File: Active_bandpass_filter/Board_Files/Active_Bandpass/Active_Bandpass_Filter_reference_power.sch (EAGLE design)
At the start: 16 parts, among them IC2 AD8031R, IC3 7805TV

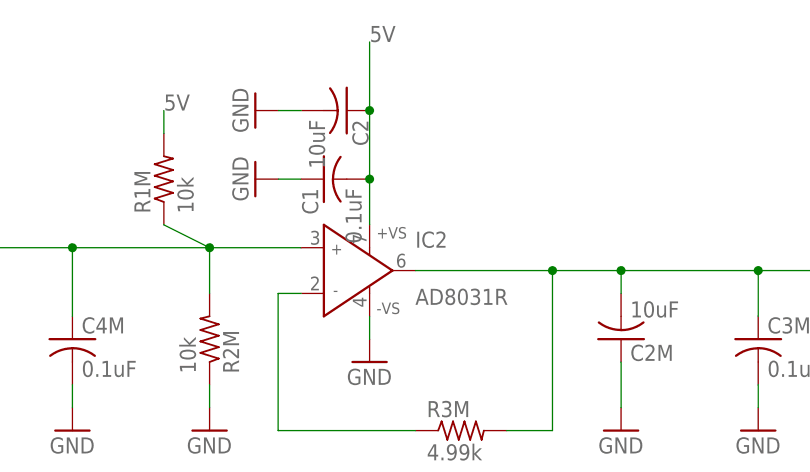
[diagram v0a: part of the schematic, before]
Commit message: reference power board routed completely
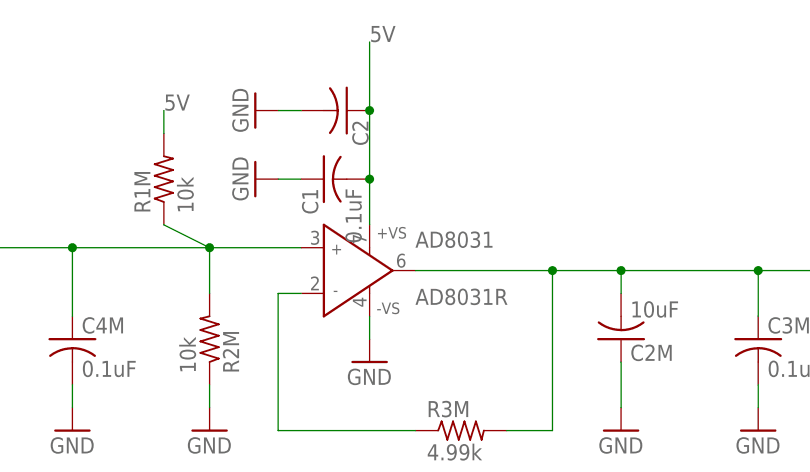
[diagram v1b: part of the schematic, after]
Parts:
- C2: value 10uF -> (none)
- renumbered IC2 to AD8031
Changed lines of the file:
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@@
 <parts>
 <part name="FRAME1" library="frames" deviceset="FRAME_A_L" device=""/>
-<part name="IC2" library="analog-devices" deviceset="AD8031" device="R"/>
+<part name="AD8031" library="analog-devices" deviceset="AD8031" device="R"/>
 <part name="R1M" library="resistor" deviceset="R-US_" device="R1206" value="10k"/>
 <part name="R2M" library="resistor" deviceset="R-US_" device="R1206" value="10k"/>
@@
 <part name="JP10" library="SparkFun-Connectors" deviceset="M03X2" device="2X3_SILK_MALE_PTH"/>
 <part name="C1" library="resistor" deviceset="C-US" device="C1206" value="0.1uF"/>
-<part name="C2" library="resistor" deviceset="C-US" device="C1206" value="10uF"/>
+<part name="C2" library="resistor" deviceset="C-US" device="C1206"/>
 <part name="C3" library="resistor" deviceset="C-US" device="C1206" value="0.1uF"/>
 <part name="C4" library="resistor" deviceset="C-US" device="C1206" value="10uF"/>
@@
 <instance part="FRAME1" gate="G$1" x="-17.78" y="-10.16"/>
 <instance part="FRAME1" gate="G$2" x="154.94" y="-10.16"/>
-<instance part="IC2" gate="P" x="101.6" y="86.36"/>
+<instance part="AD8031" gate="P" x="101.6" y="86.36"/>
 <instance part="R1M" gate="G$1" x="81.28" y="96.52" rot="R90"/>
 <instance part="R2M" gate="G$1" x="86.36" y="78.74" rot="MR90"/>
@@
 </segment>
 <segment>
-<pinref part="IC2" gate="P" pin="-VS"/>
+<pinref part="AD8031" gate="P" pin="-VS"/>
 <pinref part="GND7" gate="1" pin="GND"/>
 <wire x1="104.14" y1="81.28" x2="104.14" y2="78.74" width="0.1524" layer="91"/>
@@
 </segment>
 <segment>
-<pinref part="IC2" gate="P" pin="+VS"/>
+<pinref part="AD8031" gate="P" pin="+VS"/>
 <label x="104.14" y="111.76" size="1.778" layer="95"/>
 <pinref part="C2" gate="G$1" pin="1"/>
@@
 <pinref part="R2M" gate="G$1" pin="2"/>
 <wire x1="81.28" y1="91.44" x2="86.36" y2="88.9" width="0.1524" layer="91"/>
-<pinref part="IC2" gate="P" pin="IN+"/>
+<pinref part="AD8031" gate="P" pin="IN+"/>
 <wire x1="86.36" y1="88.9" x2="86.36" y2="83.82" width="0.1524" layer="91"/>
 <wire x1="96.52" y1="88.9" x2="86.36" y2="88.9" width="0.1524" layer="91"/>
@@
 <net name="N$12" class="0">
 <segment>
-<pinref part="IC2" gate="P" pin="IN-"/>
+<pinref part="AD8031" gate="P" pin="IN-"/>
 <wire x1="96.52" y1="83.82" x2="93.98" y2="83.82" width="0.1524" layer="91"/>
 <wire x1="93.98" y1="83.82" x2="93.98" y2="68.58" width="0.1524" layer="91"/>
@@
 <wire x1="119.38" y1="68.58" x2="124.46" y2="68.58" width="0.1524" layer="91"/>
 <wire x1="124.46" y1="68.58" x2="124.46" y2="86.36" width="0.1524" layer="91"/>
-<pinref part="IC2" gate="P" pin="OUT"/>
+<pinref part="AD8031" gate="P" pin="OUT"/>
 <wire x1="124.46" y1="86.36" x2="109.22" y2="86.36" width="0.1524" layer="91"/>
 <junction x="124.46" y="86.36"/>

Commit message: routing, DRC, Ratsnest all okay
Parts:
- renumbered C1M to C5, C2M to C7, C3M to C8, C4M to C6, R1M to R1, R2M to R2, R3M to R3
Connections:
- net N$8 renamed C5
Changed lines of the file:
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@@
 <part name="FRAME1" library="frames" deviceset="FRAME_A_L" device=""/>
 <part name="AD8031" library="analog-devices" deviceset="AD8031" device="R"/>
-<part name="R1M" library="resistor" deviceset="R-US_" device="R1206" value="10k"/>
-<part name="R2M" library="resistor" deviceset="R-US_" device="R1206" value="10k"/>
-<part name="R3M" library="rcl" deviceset="R-US_" device="R1206" value="4.99k"/>
-<part name="C4M" library="resistor" deviceset="C-US" device="C1206" value="0.1uF"/>
-<part name="C2M" library="resistor" deviceset="C-US" device="C1206" value="10uF"/>
-<part name="C3M" library="resistor" deviceset="C-US" device="C1206" value="0.1uF"/>
-<part name="C1M" library="resistor" deviceset="C-US" device="C1206" value="10uF"/>
+<part name="R1" library="resistor" deviceset="R-US_" device="R1206" value="10k"/>
+<part name="R2" library="resistor" deviceset="R-US_" device="R1206" value="10k"/>
+<part name="R3" library="rcl" deviceset="R-US_" device="R1206" value="4.99k"/>
+<part name="C6" library="resistor" deviceset="C-US" device="C1206" value="0.1uF"/>
+<part name="C7" library="resistor" deviceset="C-US" device="C1206" value="10uF"/>
+<part name="C8" library="resistor" deviceset="C-US" device="C1206" value="0.1uF"/>
+<part name="C5" library="resistor" deviceset="C-US" device="C1206" value="10uF"/>
 <part name="GND1" library="SparkFun-Aesthetics" deviceset="GND" device=""/>
 <part name="SUPPLY1" library="SparkFun-Aesthetics" deviceset="VCC" device=""/>
@@
 <instance part="FRAME1" gate="G$2" x="154.94" y="-10.16"/>
 <instance part="AD8031" gate="P" x="101.6" y="86.36"/>
-<instance part="R1M" gate="G$1" x="81.28" y="96.52" rot="R90"/>
-<instance part="R2M" gate="G$1" x="86.36" y="78.74" rot="MR90"/>
-<instance part="R3M" gate="G$1" x="114.3" y="68.58"/>
-<instance part="C4M" gate="G$1" x="71.12" y="78.74"/>
-<instance part="C2M" gate="G$1" x="132.08" y="78.74" rot="MR180"/>
-<instance part="C3M" gate="G$1" x="147.32" y="78.74"/>
-<instance part="C1M" gate="G$1" x="55.88" y="78.74"/>
+<instance part="R1" gate="G$1" x="81.28" y="96.52" rot="R90"/>
+<instance part="R2" gate="G$1" x="86.36" y="78.74" rot="MR90"/>
+<instance part="R3" gate="G$1" x="114.3" y="68.58"/>
+<instance part="C6" gate="G$1" x="71.12" y="78.74"/>
+<instance part="C7" gate="G$1" x="132.08" y="78.74" rot="MR180"/>
+<instance part="C8" gate="G$1" x="147.32" y="78.74"/>
+<instance part="C5" gate="G$1" x="55.88" y="78.74"/>
 <instance part="GND1" gate="1" x="33.02" y="76.2"/>
 <instance part="SUPPLY1" gate="G$1" x="15.24" y="96.52" rot="R90"/>
@@
 <net name="GND" class="0">
 <segment>
-<pinref part="C1M" gate="G$1" pin="2"/>
+<pinref part="C5" gate="G$1" pin="2"/>
 <pinref part="GND" gate="1" pin="GND"/>
 <wire x1="55.88" y1="73.66" x2="55.88" y2="71.12" width="0.1524" layer="91"/>
 </segment>
 <segment>
-<pinref part="C4M" gate="G$1" pin="2"/>
+<pinref part="C6" gate="G$1" pin="2"/>
 <pinref part="GND3" gate="1" pin="GND"/>
 <wire x1="71.12" y1="73.66" x2="71.12" y2="71.12" width="0.1524" layer="91"/>
 </segment>
 <segment>
-<pinref part="R2M" gate="G$1" pin="1"/>
+<pinref part="R2" gate="G$1" pin="1"/>
 <pinref part="GND4" gate="1" pin="GND"/>
 <wire x1="86.36" y1="73.66" x2="86.36" y2="71.12" width="0.1524" layer="91"/>
 </segment>
 <segment>
-<pinref part="C3M" gate="G$1" pin="2"/>
+<pinref part="C8" gate="G$1" pin="2"/>
 <pinref part="GND6" gate="1" pin="GND"/>
 <wire x1="147.32" y1="73.66" x2="147.32" y2="71.12" width="0.1524" layer="91"/>
@@
 </segment>
 <segment>
-<pinref part="C2M" gate="G$1" pin="1"/>
+<pinref part="C7" gate="G$1" pin="1"/>
 <pinref part="GND5" gate="1" pin="GND"/>
 <wire x1="132.08" y1="76.2" x2="132.08" y2="71.12" width="0.1524" layer="91"/>
@@
 </segment>
 <segment>
-<pinref part="R1M" gate="G$1" pin="2"/>
+<pinref part="R1" gate="G$1" pin="2"/>
 <wire x1="81.28" y1="101.6" x2="81.28" y2="104.14" width="0.1524" layer="91"/>
 <label x="81.28" y="104.14" size="1.778" layer="95"/>
@@
 </segment>
 </net>
-<net name="N$8" class="0">
-<segment>
-<pinref part="R1M" gate="G$1" pin="1"/>
-<pinref part="R2M" gate="G$1" pin="2"/>
+<net name="C5" class="0">
+<segment>
+<pinref part="R1" gate="G$1" pin="1"/>
+<pinref part="R2" gate="G$1" pin="2"/>
 <wire x1="81.28" y1="91.44" x2="86.36" y2="88.9" width="0.1524" layer="91"/>
 <pinref part="AD8031" gate="P" pin="IN+"/>
@@
 <wire x1="96.52" y1="88.9" x2="86.36" y2="88.9" width="0.1524" layer="91"/>
 <junction x="86.36" y="88.9"/>
-<pinref part="C4M" gate="G$1" pin="1"/>
+<pinref part="C6" gate="G$1" pin="1"/>
 <wire x1="86.36" y1="88.9" x2="71.12" y2="88.9" width="0.1524" layer="91"/>
 <wire x1="71.12" y1="88.9" x2="71.12" y2="81.28" width="0.1524" layer="91"/>
-<pinref part="C1M" gate="G$1" pin="1"/>
+<pinref part="C5" gate="G$1" pin="1"/>
 <wire x1="71.12" y1="88.9" x2="55.88" y2="88.9" width="0.1524" layer="91"/>
 <wire x1="55.88" y1="88.9" x2="55.88" y2="81.28" width="0.1524" layer="91"/>
@@
 <wire x1="96.52" y1="83.82" x2="93.98" y2="83.82" width="0.1524" layer="91"/>
 <wire x1="93.98" y1="83.82" x2="93.98" y2="68.58" width="0.1524" layer="91"/>
-<pinref part="R3M" gate="G$1" pin="1"/>
+<pinref part="R3" gate="G$1" pin="1"/>
 <wire x1="93.98" y1="68.58" x2="109.22" y2="68.58" width="0.1524" layer="91"/>
 </segment>
@@
 <net name="REF" class="0">
 <segment>
-<pinref part="R3M" gate="G$1" pin="2"/>
+<pinref part="R3" gate="G$1" pin="2"/>
 <wire x1="119.38" y1="68.58" x2="124.46" y2="68.58" width="0.1524" layer="91"/>
 <wire x1="124.46" y1="68.58" x2="124.46" y2="86.36" width="0.1524" layer="91"/>
@@
 <wire x1="124.46" y1="86.36" x2="109.22" y2="86.36" width="0.1524" layer="91"/>
 <junction x="124.46" y="86.36"/>
-<pinref part="C3M" gate="G$1" pin="1"/>
+<pinref part="C8" gate="G$1" pin="1"/>
 <wire x1="124.46" y1="86.36" x2="132.08" y2="86.36" width="0.1524" layer="91"/>
 <wire x1="132.08" y1="86.36" x2="147.32" y2="86.36" width="0.1524" layer="91"/>
@@
 <label x="157.48" y="86.36" size="1.778" layer="95"/>
 <wire x1="147.32" y1="86.36" x2="157.48" y2="86.36" width="0.1524" layer="91"/>
-<pinref part="C2M" gate="G$1" pin="2"/>
+<pinref part="C7" gate="G$1" pin="2"/>
 <wire x1="132.08" y1="83.82" x2="132.08" y2="86.36" width="0.1524" layer="91"/>
 <junction x="132.08" y="86.36"/>
@@
 </sheet>
 </sheets>
+<errors>
+</errors>
 </schematic>
 </drawing>
